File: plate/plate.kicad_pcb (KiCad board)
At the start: 2 copper layers, 499.9 x 141.3 mm, 122 parts

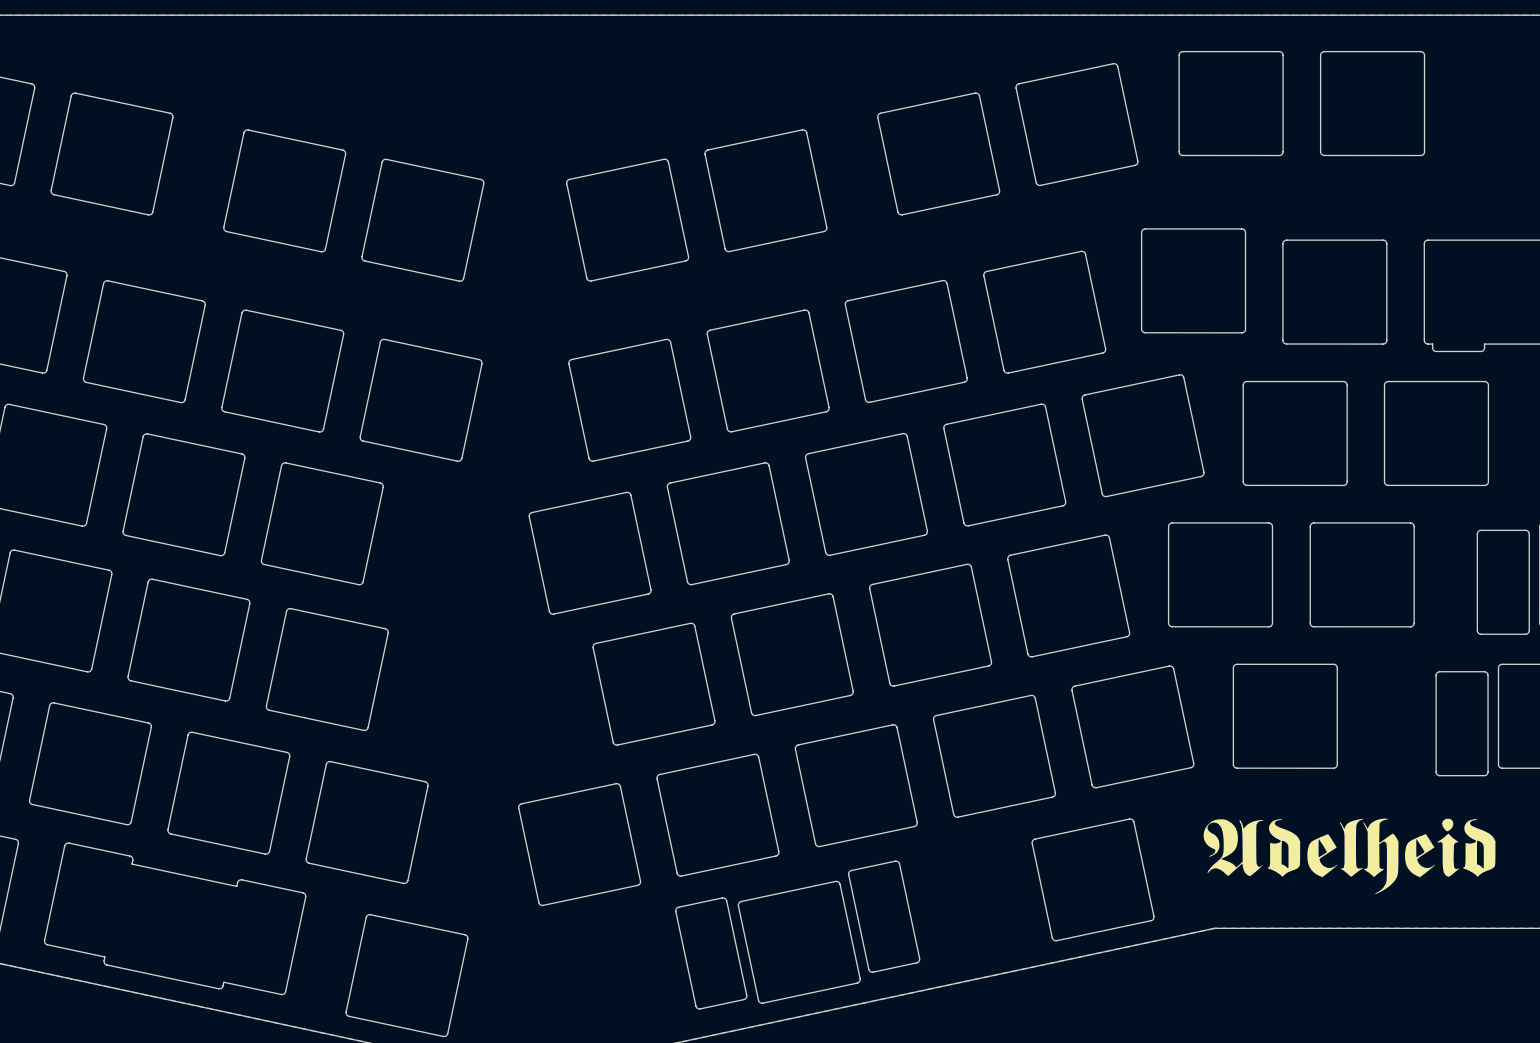
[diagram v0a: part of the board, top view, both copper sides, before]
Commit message: fix D1 and space stab holes
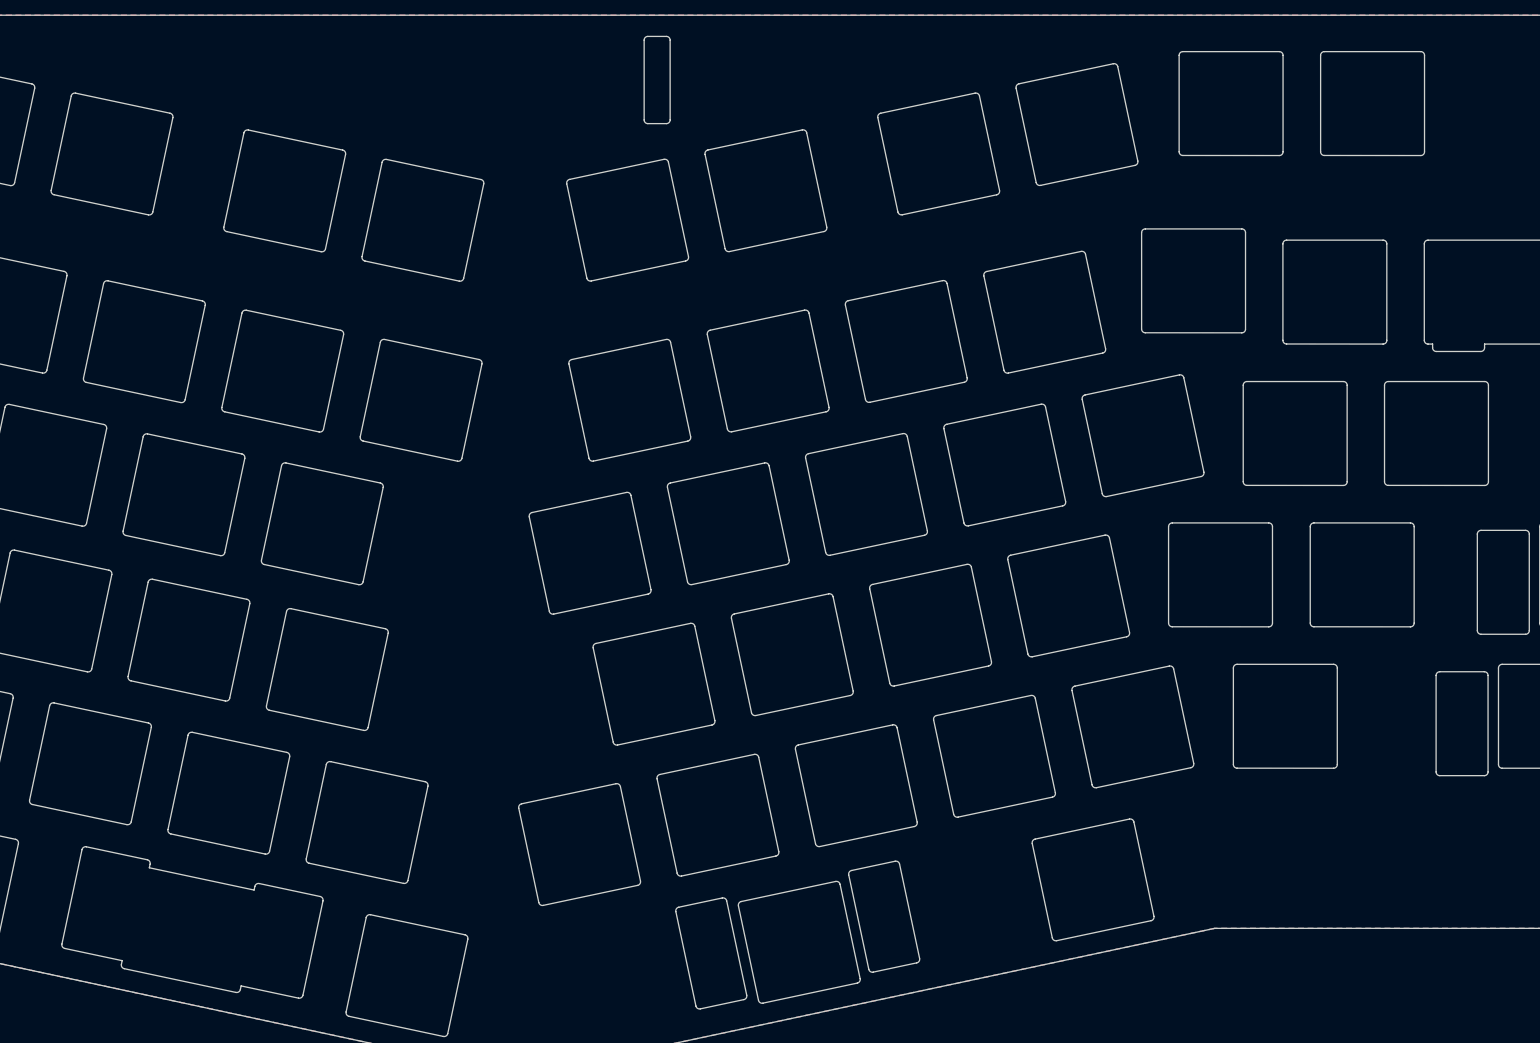
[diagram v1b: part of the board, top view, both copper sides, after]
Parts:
- removed G1: LOGO, adelheid:adelheid-logo
- removed the REF** at (146.7, 347.6)
- added H100: OLED_Header, Custom_Footprints:SSD1306_OLED, F.Cu at (192.9, 233.4)
- added REF**: MX225, acheron_MX_PlateSlots:MX225, F.Cu at (146.7, 347.6)
